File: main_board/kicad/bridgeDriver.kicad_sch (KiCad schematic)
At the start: 16 parts, among them U9 IR2133

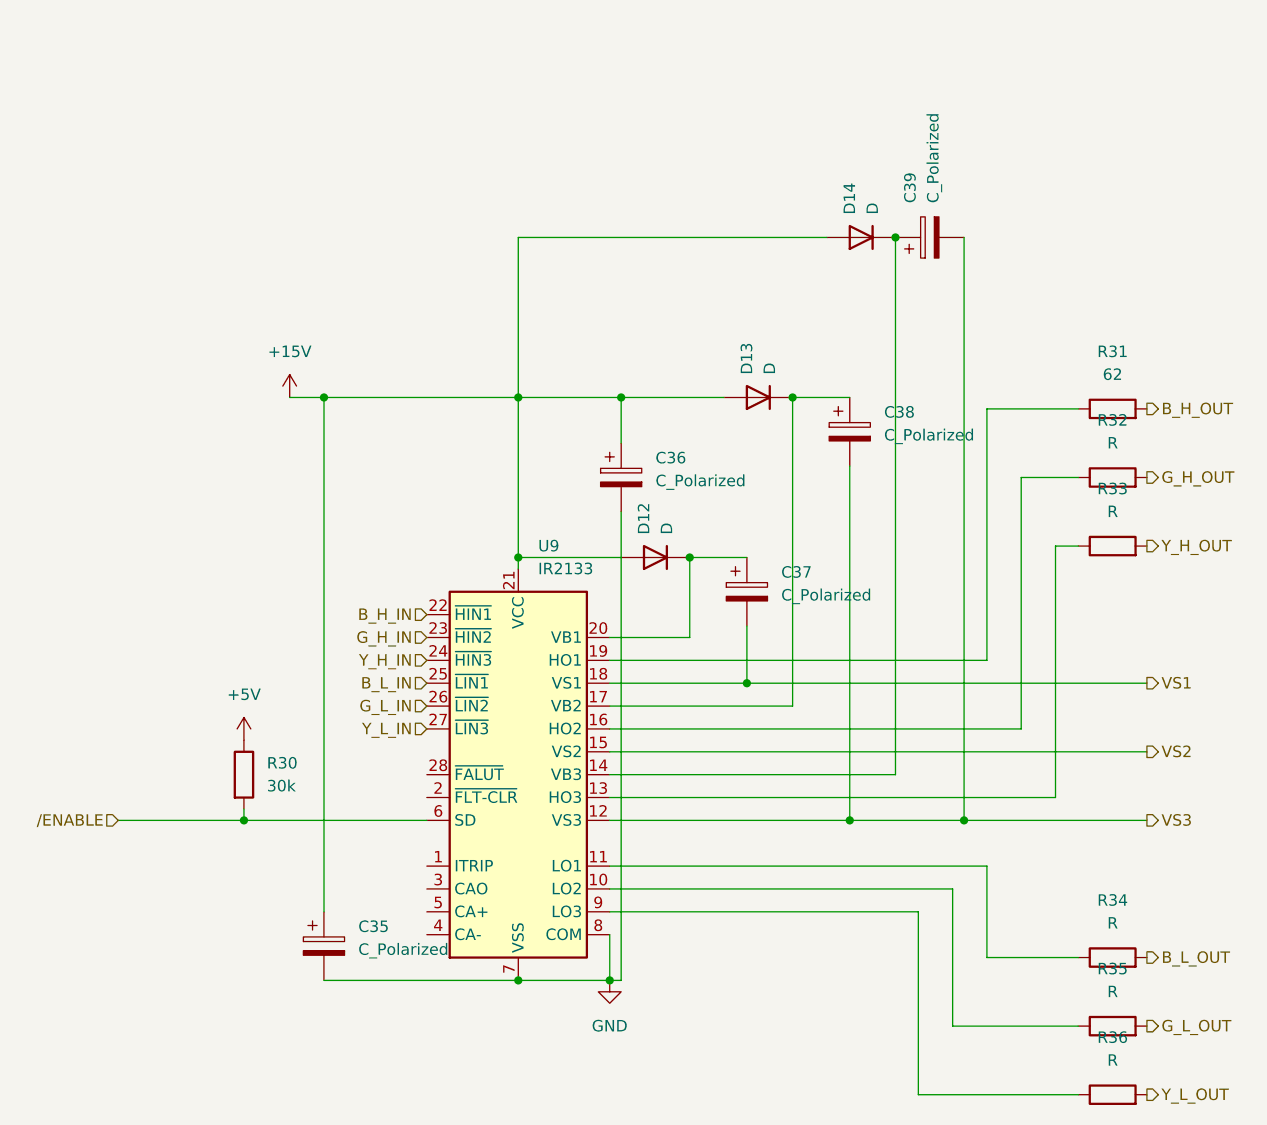
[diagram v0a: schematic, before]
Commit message: added bridge driver values
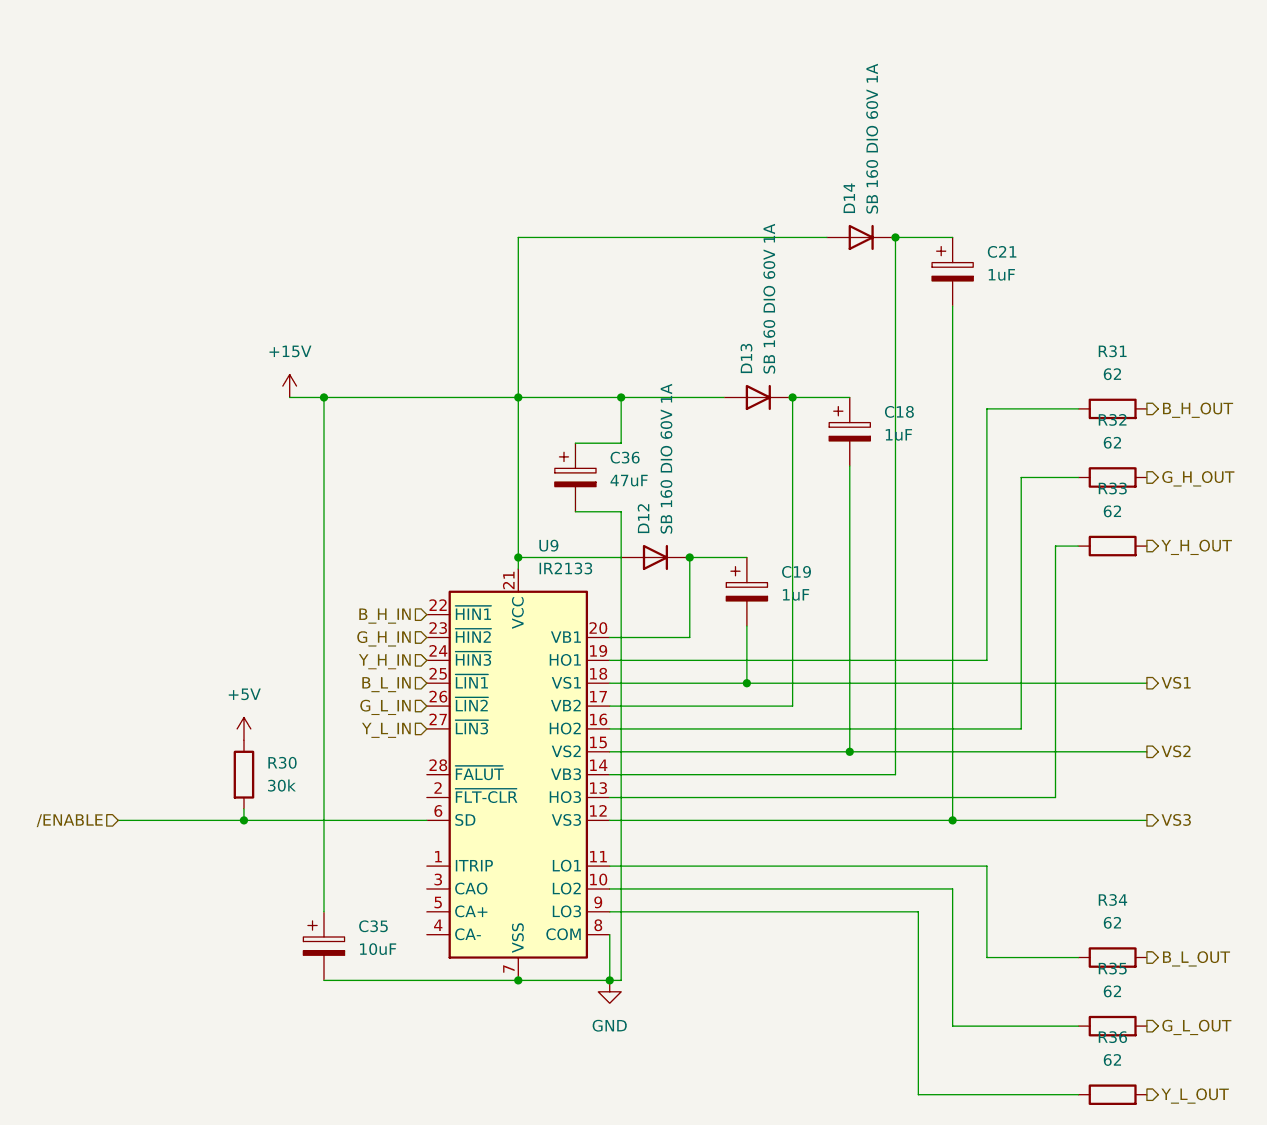
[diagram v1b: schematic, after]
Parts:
- removed C37, C38, C39: C_Polarized, symbol Device:C_Polarized
- added C18, C19, C21: 1uF, symbol Device:C_Polarized
- C35: value C_Polarized -> 10uF
- C36: value C_Polarized -> 47uF
- D12, D13, D14: value D -> SB 160 DIO 60V 1A
- R32, R33, R34, R35, R36: value R -> 62
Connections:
- net VS1: now also C19.2
- net VS2: now also C18.2
- net VS3: now also C21.2
- net at D14.1 (K), U9.14 (VB3): now also C21.1
- net at D13.1 (K), U9.17 (VB2): now also C18.1
- net at D12.1 (K), U9.20 (VB1): now also C19.1
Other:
- moved on the sheet: C36

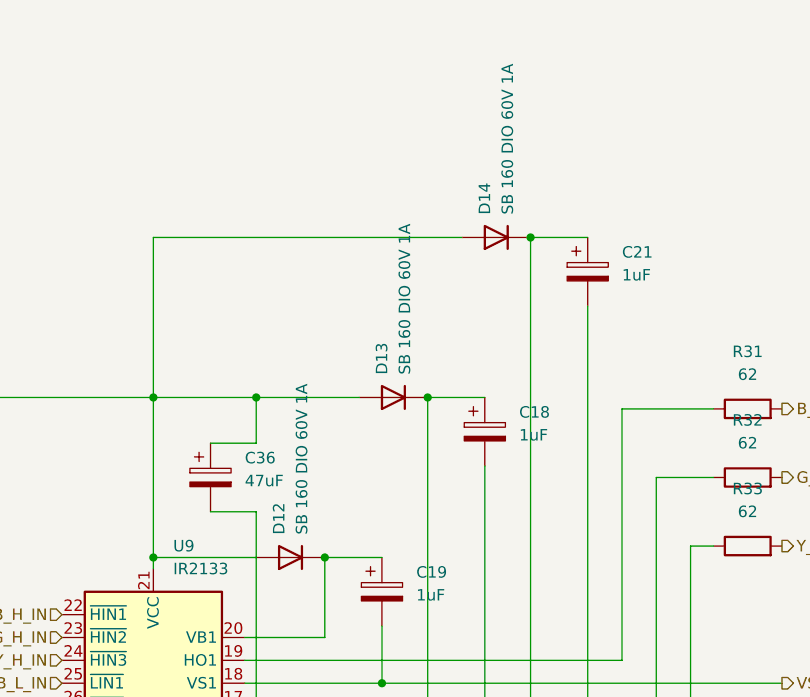
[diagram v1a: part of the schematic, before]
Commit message: added eeprom values
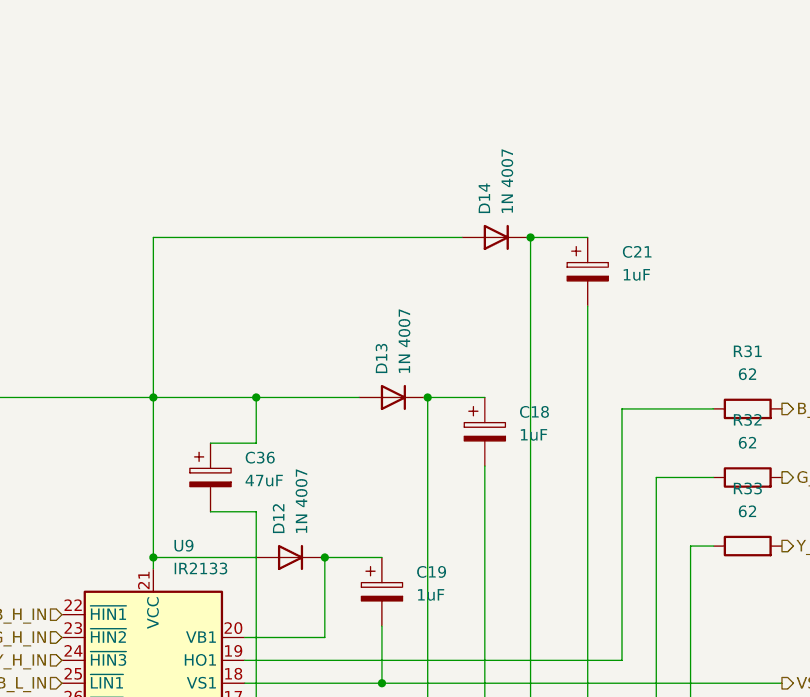
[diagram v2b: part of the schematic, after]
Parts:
- D12, D13, D14: value SB 160 DIO 60V 1A -> 1N 4007
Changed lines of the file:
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@@
       (effects (font (size 1.27 1.27)) (justify right))
     )
-    (property "Value" "SB 160 DIO 60V 1A" (at 161.29 60.96 90)
+    (property "Value" "1N 4007" (at 161.29 60.96 90)
       (effects (font (size 1.27 1.27)) (justify right))
     )
@@
       (effects (font (size 1.27 1.27)) (justify right))
     )
-    (property "Value" "SB 160 DIO 60V 1A" (at 172.72 43.18 90)
+    (property "Value" "1N 4007" (at 172.72 43.18 90)
       (effects (font (size 1.27 1.27)) (justify right))
     )
@@
       (effects (font (size 1.27 1.27)) (justify right))
     )
-    (property "Value" "SB 160 DIO 60V 1A" (at 149.86 78.74 90)
-      (effects (font (size 1.27 1.27)) (justify right))
-    )
+    (property "Value" "1N 4007" (at 149.86 78.74 90)
+      (effects (font (size 1.27 1.27)) (justify right))
+    )

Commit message: renamed motor magic file
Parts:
- renumbered C35 to C14, C36 to C15, C19 to C16, C18 to C17, C21 to C20, D13 to D10, D14 to D11, D12 to D9, R30 to R14, R31 to R15, R32 to R16, R33 to R17, R34 to R18, R35 to R19, R36 to R20, U9 to U5

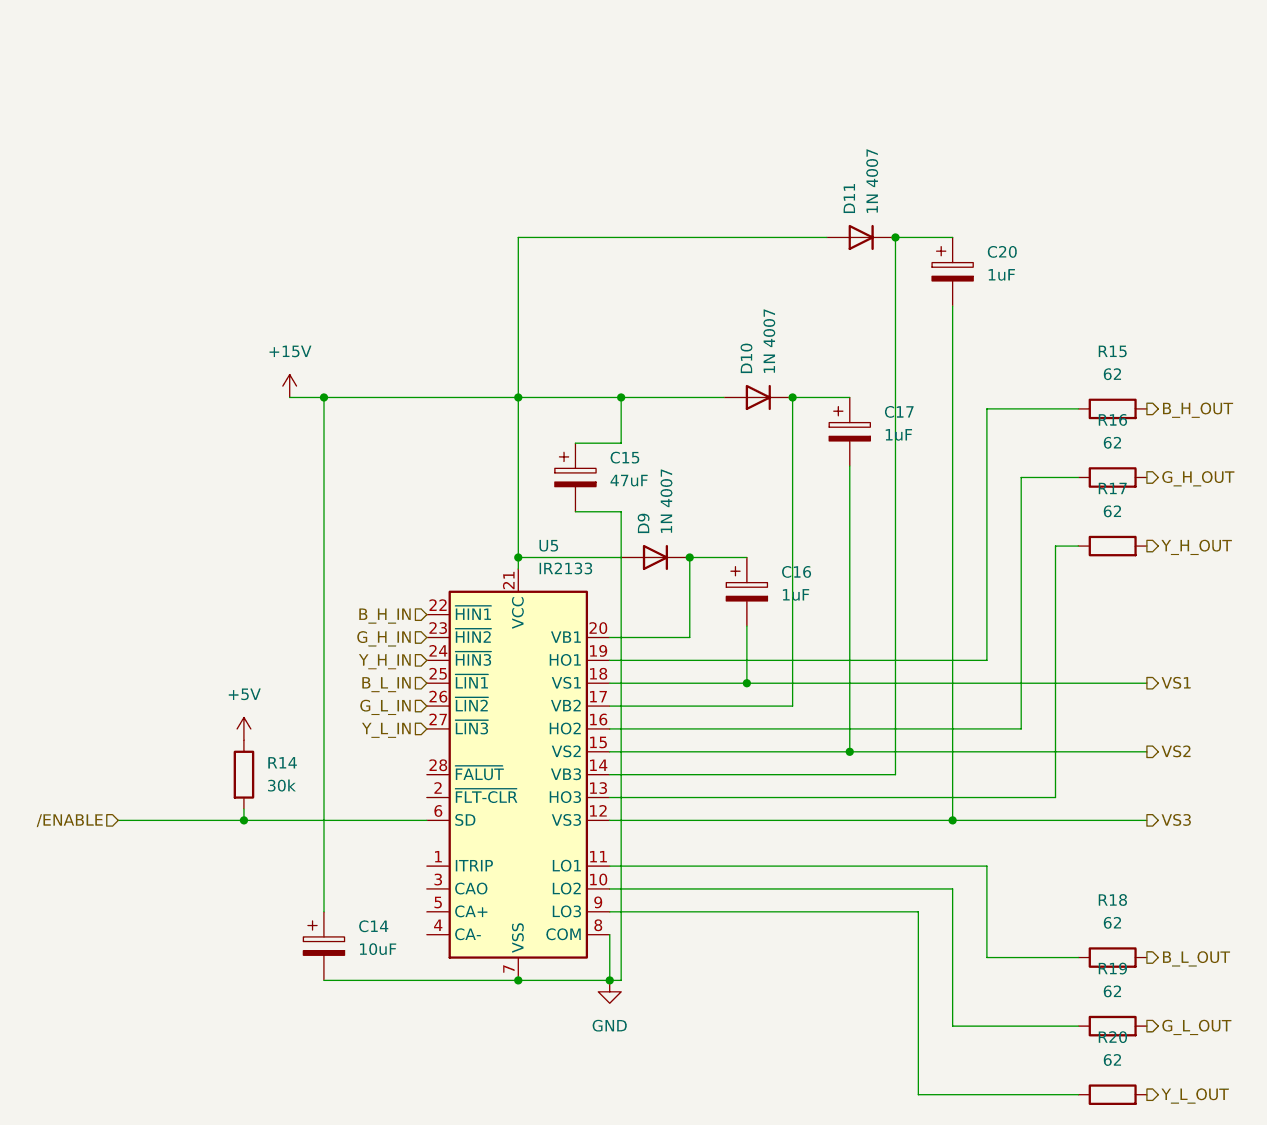
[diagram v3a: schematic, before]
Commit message: added LEDS and fuses
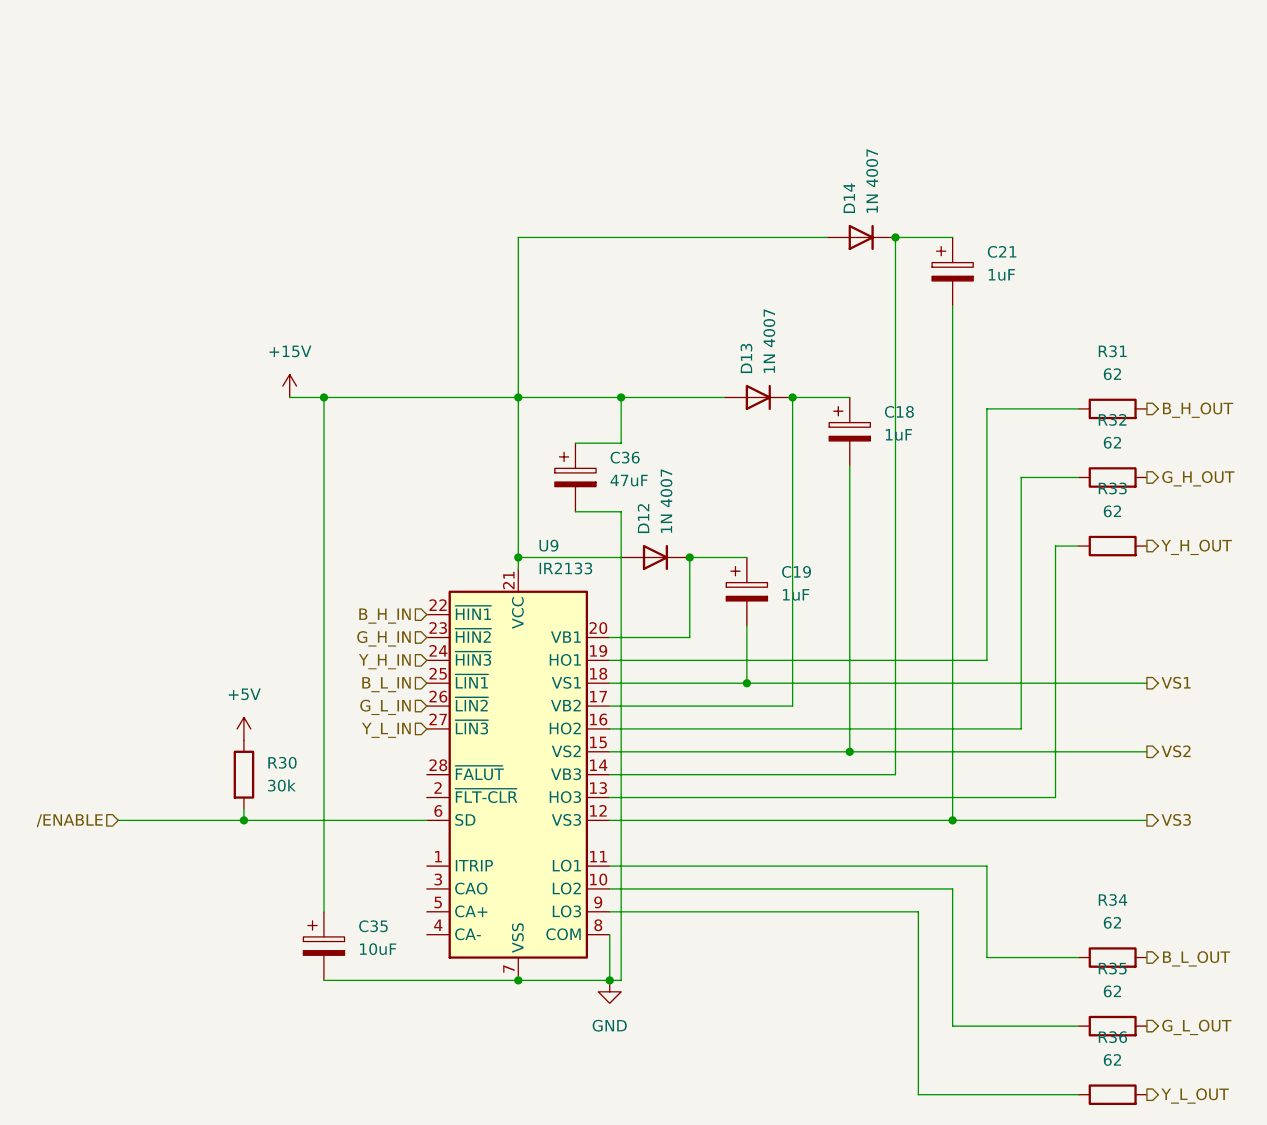
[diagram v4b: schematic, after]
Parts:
- renumbered C17 to C18, C16 to C19, C20 to C21, C14 to C35, C15 to C36, D9 to D12, D10 to D13, D11 to D14, R14 to R30, R15 to R31, R16 to R32, R17 to R33, R18 to R34, R19 to R35, R20 to R36, U5 to U9
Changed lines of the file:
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@@
   (symbol (lib_id "power:+15V") (at 107.95 63.5 0) (unit 1)
     (in_bom yes) (on_board yes) (dnp no) (fields_autoplaced)
-    (property "Reference" "#PWR031" (at 107.95 67.31 0)
+    (property "Reference" "#PWR063" (at 107.95 67.31 0)
       (effects (font (size 1.27 1.27)) hide)
     )
@@
   (symbol (lib_id "Driver_FET:IR2133") (at 133.35 105.41 0) (unit 1)
     (in_bom yes) (on_board yes) (dnp no) (fields_autoplaced)
-    (property "Reference" "U5" (at 135.5441 80.01 0)
+    (property "Reference" "U9" (at 135.5441 80.01 0)
       (effects (font (size 1.27 1.27)) (justify left))
     )
@@
   (symbol (lib_id "Device:R") (at 199.39 72.39 90) (unit 1)
     (in_bom yes) (on_board yes) (dnp no) (fields_autoplaced)
-    (property "Reference" "R16" (at 199.39 66.04 90)
+    (property "Reference" "R32" (at 199.39 66.04 90)
       (effects (font (size 1.27 1.27)))
     )
@@
   (symbol (lib_id "power:GND") (at 143.51 128.27 0) (unit 1)
     (in_bom yes) (on_board yes) (dnp no) (fields_autoplaced)
-    (property "Reference" "#PWR032" (at 143.51 134.62 0)
+    (property "Reference" "#PWR064" (at 143.51 134.62 0)
       (effects (font (size 1.27 1.27)) hide)
     )
@@
   (symbol (lib_id "Device:R") (at 199.39 64.77 90) (unit 1)
     (in_bom yes) (on_board yes) (dnp no) (fields_autoplaced)
-    (property "Reference" "R15" (at 199.39 58.42 90)
+    (property "Reference" "R31" (at 199.39 58.42 90)
       (effects (font (size 1.27 1.27)))
     )
@@
   (symbol (lib_id "Device:C_Polarized") (at 170.18 67.31 0) (unit 1)
     (in_bom yes) (on_board yes) (dnp no) (fields_autoplaced)
-    (property "Reference" "C17" (at 173.99 65.151 0)
+    (property "Reference" "C18" (at 173.99 65.151 0)
       (effects (font (size 1.27 1.27)) (justify left))
     )
@@
   (symbol (lib_id "Device:R") (at 102.87 105.41 0) (unit 1)
     (in_bom yes) (on_board yes) (dnp no) (fields_autoplaced)
-    (property "Reference" "R14" (at 105.41 104.14 0)
+    (property "Reference" "R30" (at 105.41 104.14 0)
       (effects (font (size 1.27 1.27)) (justify left))
     )
@@
   (symbol (lib_id "Device:C_Polarized") (at 111.76 124.46 0) (unit 1)
     (in_bom yes) (on_board yes) (dnp no) (fields_autoplaced)
-    (property "Reference" "C14" (at 115.57 122.301 0)
+    (property "Reference" "C35" (at 115.57 122.301 0)
       (effects (font (size 1.27 1.27)) (justify left))
     )
@@
   (symbol (lib_id "Device:D") (at 160.02 63.5 180) (unit 1)
     (in_bom yes) (on_board yes) (dnp no) (fields_autoplaced)
-    (property "Reference" "D10" (at 158.75 60.96 90)
+    (property "Reference" "D13" (at 158.75 60.96 90)
       (effects (font (size 1.27 1.27)) (justify right))
     )
@@
   (symbol (lib_id "Device:C_Polarized") (at 158.75 85.09 0) (unit 1)
     (in_bom yes) (on_board yes) (dnp no) (fields_autoplaced)
-    (property "Reference" "C16" (at 162.56 82.931 0)
+    (property "Reference" "C19" (at 162.56 82.931 0)
       (effects (font (size 1.27 1.27)) (justify left))
     )
@@
   (symbol (lib_id "Device:D") (at 171.45 45.72 180) (unit 1)
     (in_bom yes) (on_board yes) (dnp no) (fields_autoplaced)
-    (property "Reference" "D11" (at 170.18 43.18 90)
+    (property "Reference" "D14" (at 170.18 43.18 90)
       (effects (font (size 1.27 1.27)) (justify right))
     )
@@
   (symbol (lib_id "power:+5V") (at 102.87 101.6 0) (unit 1)
     (in_bom yes) (on_board yes) (dnp no) (fields_autoplaced)
-    (property "Reference" "#PWR030" (at 102.87 105.41 0)
+    (property "Reference" "#PWR062" (at 102.87 105.41 0)
       (effects (font (size 1.27 1.27)) hide)
     )
@@
   (symbol (lib_id "Device:C_Polarized") (at 139.7 72.39 0) (unit 1)
     (in_bom yes) (on_board yes) (dnp no) (fields_autoplaced)
-    (property "Reference" "C15" (at 143.51 70.231 0)
+    (property "Reference" "C36" (at 143.51 70.231 0)
       (effects (font (size 1.27 1.27)) (justify left))
     )
@@
   (symbol (lib_id "Device:R") (at 199.39 133.35 90) (unit 1)
     (in_bom yes) (on_board yes) (dnp no) (fields_autoplaced)
-    (property "Reference" "R19" (at 199.39 127 90)
+    (property "Reference" "R35" (at 199.39 127 90)
       (effects (font (size 1.27 1.27)))
     )
@@
   (symbol (lib_id "Device:R") (at 199.39 80.01 90) (unit 1)
     (in_bom yes) (on_board yes) (dnp no) (fields_autoplaced)
-    (property "Reference" "R17" (at 199.39 73.66 90)
+    (property "Reference" "R33" (at 199.39 73.66 90)
       (effects (font (size 1.27 1.27)))
     )
@@
   (symbol (lib_id "Device:C_Polarized") (at 181.61 49.53 0) (unit 1)
     (in_bom yes) (on_board yes) (dnp no) (fields_autoplaced)
-    (property "Reference" "C20" (at 185.42 47.371 0)
+    (property "Reference" "C21" (at 185.42 47.371 0)
       (effects (font (size 1.27 1.27)) (justify left))
     )
@@
   (symbol (lib_id "Device:R") (at 199.39 140.97 90) (unit 1)
     (in_bom yes) (on_board yes) (dnp no) (fields_autoplaced)
-    (property "Reference" "R20" (at 199.39 134.62 90)
+    (property "Reference" "R36" (at 199.39 134.62 90)
       (effects (font (size 1.27 1.27)))
     )
@@
   (symbol (lib_id "Device:D") (at 148.59 81.28 180) (unit 1)
     (in_bom yes) (on_board yes) (dnp no) (fields_autoplaced)
-    (property "Reference" "D9" (at 147.32 78.74 90)
+    (property "Reference" "D12" (at 147.32 78.74 90)
       (effects (font (size 1.27 1.27)) (justify right))
     )
@@
   (symbol (lib_id "Device:R") (at 199.39 125.73 90) (unit 1)
     (in_bom yes) (on_board yes) (dnp no) (fields_autoplaced)
-    (property "Reference" "R18" (at 199.39 119.38 90)
-      (effects (font (size 1.27 1.27)))
-    )
+    (property "Reference" "R34" (at 199.39 119.38 90)
+      (effects (font (size 1.27 1.27)))
+    )
